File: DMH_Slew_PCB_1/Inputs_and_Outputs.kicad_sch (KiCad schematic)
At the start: 35 parts, among them J1 TS_Jack_6.35mm_Sw, J10 TS_Jack_6.35mm_Sw, J11 TS_Jack_6.35mm_Sw, J2 TS_Jack_6.35mm_Sw, J200 IDC_02x05, J3 TS_Jack_6.35mm_Sw, J4 TS_Jack_6.35mm_Sw, J5 TS_Jack_6.35mm_Sw, J6 TS_Jack_6.35mm_Sw, J7 TS_Jack_6.35mm_Sw, J8 TS_Jack_6.35mm_Sw, J9 TS_Jack_6.35mm_Sw, SW3 SW_SPDT, U1 TL074, U2 TL072, U5 CD4053B, U6 CD4053B

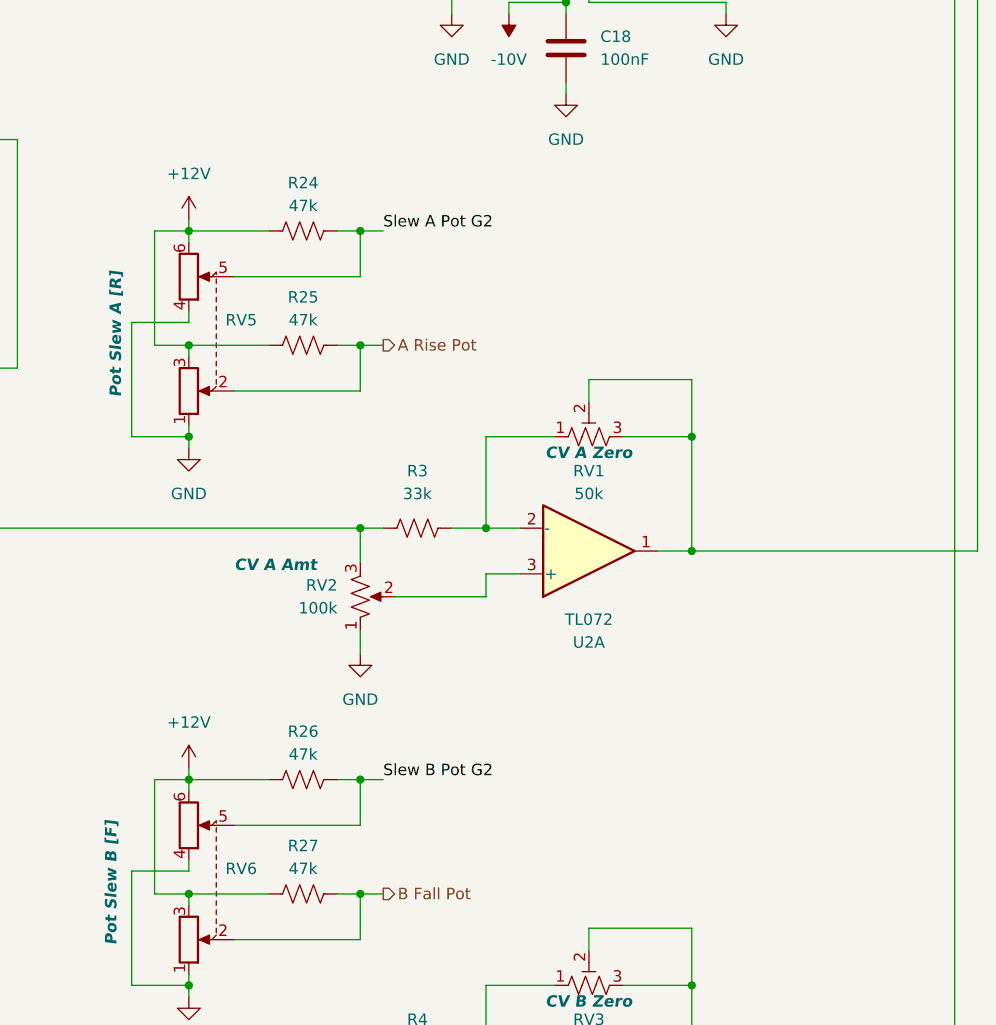
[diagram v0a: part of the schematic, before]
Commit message: Applied 10V to pots
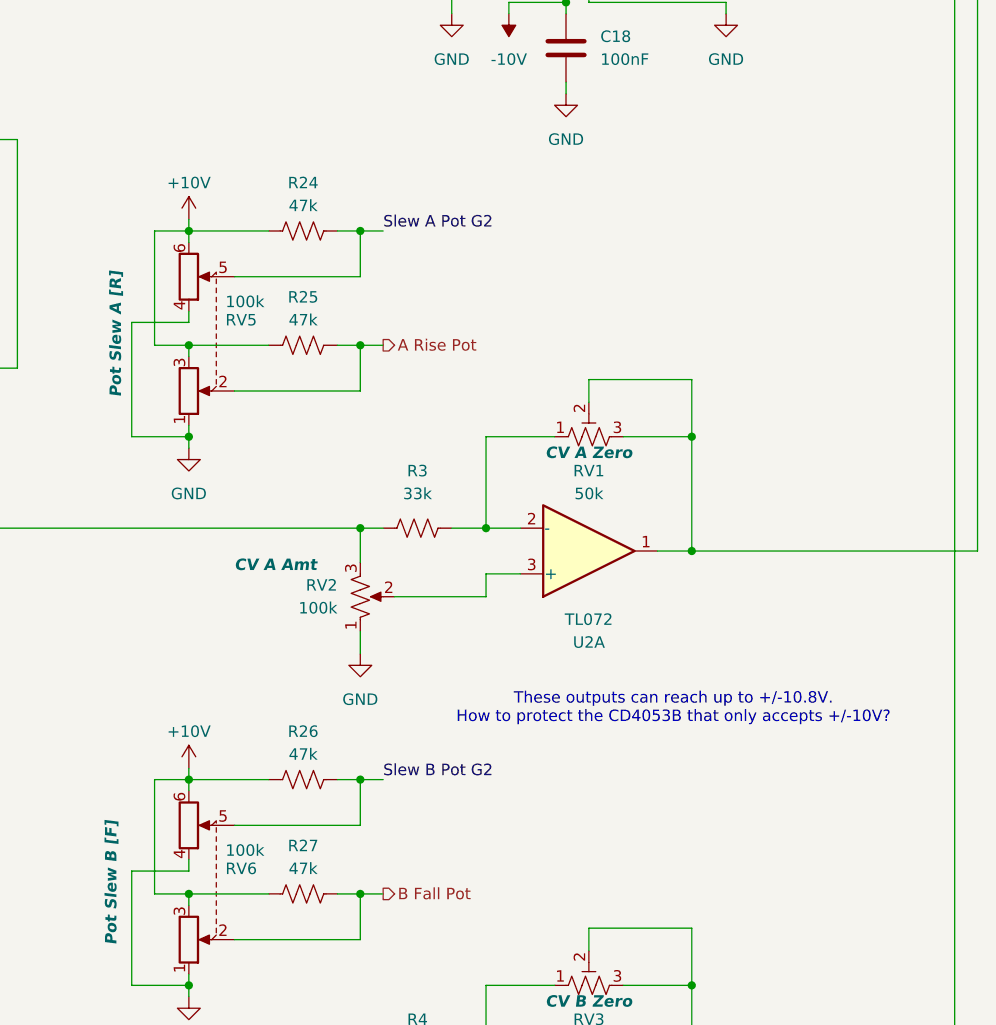
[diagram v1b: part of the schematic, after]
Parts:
- RV5, RV6: value R_Potentiometer_Dual -> 100k
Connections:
- net +12V is gone; now on net +10V: R24.1, R25.1, R26.1, R27.1, RV5.3, RV5.6, RV6.3, RV6.6
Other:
- note added: "These outputs can reach up to +/-10.8V. How to protect the CD4053B that only accepts +/-10V?"
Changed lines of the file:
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@@
 		(comment 1 "PCB for 5 cm Kosmo format synthesizer module")
 	)
+	(text "These outputs can reach up to +/-10.8V.\nHow to protect the CD4053B that only accepts +/-10V?"
+		(exclude_from_sim no)
+		(at 161.798 192.786 0)
+		(effects
+			(font
+				(size 1.27 1.27)
+			)
+		)
+	)
 	(junction
 		(at 127 139.7)
@@
 	)
 	(symbol
+		(lib_id "power:+10V")
+		(at 107.95 138.43 0)
+		(unit 1)
+		(exclude_from_sim no)
+		(in_bom yes)
+		(on_board yes)
+		(dnp no)
+		(property "Reference" "#PWR024"
+			(at 107.95 142.24 0)
+			(effects
+				(font
+					(size 1.27 1.27)
+				)
+				(hide yes)
+			)
+		)
+		(property "Value" "+10V"
+			(at 107.95 134.366 0)
+			(effects
+				(font
+					(size 1.27 1.27)
+				)
+			)
+		)
+		(property "Footprint" ""
+			(at 107.95 138.43 0)
+			(effects
+				(font
+					(size 1.27 1.27)
+				)
+				(hide yes)
+			)
+		)
+		(property "Datasheet" ""
+			(at 107.95 138.43 0)
+			(effects
+				(font
+					(size 1.27 1.27)
+				)
+				(hide yes)
+			)
+		)
+		(property "Description" "Power symbol creates a global label with name \"+10V\""
+			(at 107.95 138.43 0)
+			(effects
+				(font
+					(size 1.27 1.27)
+				)
+				(hide yes)
+			)
+		)
+		(pin "1"
+		)
+		(instances
+			(project "DMH_Slew_PCB_1"
+				(path "/58f4306d-5387-4983-bb08-41a2313fd315/ce3fef8b-9f1d-4178-b50b-4a046c030679"
+					(reference "#PWR024")
+					(unit 1)
+				)
+			)
+		)
+	)
+	(symbol
 		(lib_id "Device:R_US")
 		(at 120.65 152.4 90)
@@
 	)
 	(symbol
-		(lib_id "SynthStuff:TS_Jack_6.35mm_Sw")
-		(at 25.4 152.4 0)
+		(lib_id "power:+10V")
+		(at 107.95 199.39 0)
 		(unit 1)
 		(exclude_from_sim no)
@@
 		(on_board yes)
 		(dnp no)
-		(property "Reference" "J6"
-			(at 24.765 143.51 0)
+		(property "Reference" "#PWR026"
+			(at 107.95 203.2 0)
 			(effects
 				(font
 					(size 1.27 1.27)
 				)
+				(hide yes)
 			)
 		)
-		(property "Value" "TS_Jack_6.35mm_Sw"
-			(at 24.765 146.05 0)
+		(property "Value" "+10V"
+			(at 107.95 195.326 0)
 			(effects
 				(font
@@
 			)
 		)
-		(property "Footprint" "SynthStuff:CUI_MJ-63052A"
-			(at 25.4 152.4 0)
+		(property "Footprint" ""
+			(at 107.95 199.39 0)
 			(effects
 				(font
@@
 			)
 		)
-		(property "Datasheet" "~"
-			(at 25.4 152.4 0)
+		(property "Datasheet" ""
+			(at 107.95 199.39 0)
 			(effects
 				(font
@@
 			)
 		)
-		(property "Description" "Audio Jack, 2 Poles (Mono / TS), Switched T Pole (Normalling), 6.35mm, 1/4inch"
-			(at 25.4 152.4 0)
+		(property "Description" "Power symbol creates a global label with name \"+10V\""
+			(at 107.95 199.39 0)
 			(effects
 				(font
@@
 			)
 		)
-		(property "Function" "Slew A In"
-			(at 25.4 159.512 0)
-			(effects
-				(font
-					(size 1.27 1.27)
-					(thickness 0.254)
-					(bold yes)
-					(italic yes)
-				)
-			)
-		)
-		(pin "TN"
-		)
-		(pin "S"
-		)
-		(pin "T"
+		(pin "1"
 		)
 		(instances
 			(project "DMH_Slew_PCB_1"
 				(path "/58f4306d-5387-4983-bb08-41a2313fd315/ce3fef8b-9f1d-4178-b50b-4a046c030679"
-					(reference "J6")
+					(reference "#PWR026")
 					(unit 1)
 				)
@@
 	)
 	(symbol
-		(lib_id "power:+12V")
-		(at 107.95 138.43 0)
+		(lib_id "SynthStuff:TS_Jack_6.35mm_Sw")
+		(at 25.4 152.4 0)
 		(unit 1)
 		(exclude_from_sim no)
@@
 		(on_board yes)
 		(dnp no)
-		(fields_autoplaced yes)
-		(property "Reference" "#PWR024"
-			(at 107.95 142.24 0)
+		(property "Reference" "J6"
+			(at 24.765 143.51 0)
 			(effects
 				(font
 					(size 1.27 1.27)
 				)
-				(hide yes)
 			)
 		)
-		(property "Value" "+12V"
-			(at 107.95 133.35 0)
+		(property "Value" "TS_Jack_6.35mm_Sw"
+			(at 24.765 146.05 0)
 			(effects
 				(font
@@
 			)
 		)
-		(property "Footprint" ""
-			(at 107.95 138.43 0)
+		(property "Footprint" "SynthStuff:CUI_MJ-63052A"
+			(at 25.4 152.4 0)
 			(effects
 				(font
@@
 			)
 		)
-		(property "Datasheet" ""
-			(at 107.95 138.43 0)
+		(property "Datasheet" "~"
+			(at 25.4 152.4 0)
 			(effects
 				(font
@@
 			)
 		)
-		(property "Description" "Power symbol creates a global label with name \"+12V\""
-			(at 107.95 138.43 0)
+		(property "Description" "Audio Jack, 2 Poles (Mono / TS), Switched T Pole (Normalling), 6.35mm, 1/4inch"
+			(at 25.4 152.4 0)
 			(effects
 				(font
@@
 			)
 		)
-		(pin "1"
+		(property "Function" "Slew A In"
+			(at 25.4 159.512 0)
+			(effects
+				(font
+					(size 1.27 1.27)
+					(thickness 0.254)
+					(bold yes)
+					(italic yes)
+				)
+			)
+		)
+		(pin "TN"
+		)
+		(pin "S"
+		)
+		(pin "T"
 		)
 		(instances
 			(project "DMH_Slew_PCB_1"
 				(path "/58f4306d-5387-4983-bb08-41a2313fd315/ce3fef8b-9f1d-4178-b50b-4a046c030679"
-					(reference "#PWR024")
+					(reference "J6")
 					(unit 1)
 				)
@@
 			)
 		)
-		(property "Value" "R_Potentiometer_Dual"
-			(at 112.776 208.534 90)
+		(property "Value" "100k"
+			(at 112.014 208.534 90)
 			(effects
 				(font
@@
 				)
 				(justify left)
-				(hide yes)
 			)
 		)
@@
 			)
 		)
-		(property "Value" "R_Potentiometer_Dual"
-			(at 112.776 147.574 90)
+		(property "Value" "100k"
+			(at 112.014 147.574 90)
 			(effects
 				(font
@@
 				)
 				(justify left)
-				(hide yes)
 			)
 		)
@@
 					(unit 1)
 				)
-			)
-		)
-	)
-	(symbol
-		(lib_id "power:+12V")
-		(at 107.95 199.39 0)
-		(unit 1)
-		(exclude_from_sim no)
-		(in_bom yes)
-		(on_board yes)
-		(dnp no)
-		(fields_autoplaced yes)
-		(property "Reference" "#PWR026"
-			(at 107.95 203.2 0)
-			(effects
-				(font
-					(size 1.27 1.27)
-				)
-				(hide yes)
-			)
-		)
-		(property "Value" "+12V"
-			(at 107.95 194.31 0)
-			(effects
-				(font
-					(size 1.27 1.27)
-				)
-			)
-		)
-		(property "Footprint" ""
-			(at 107.95 199.39 0)
-			(effects
-				(font
-					(size 1.27 1.27)
-				)
-				(hide yes)
-			)
-		)
-		(property "Datasheet" ""
-			(at 107.95 199.39 0)
-			(effects
-				(font
-					(size 1.27 1.27)
-				)
-				(hide yes)
-			)
-		)
-		(property "Description" "Power symbol creates a global label with name \"+12V\""
-			(at 107.95 199.39 0)
-			(effects
-				(font
-					(size 1.27 1.27)
-				)
-				(hide yes)
-			)
-		)
-		(pin "1"
-		)
-		(instances
-			(project "DMH_Slew_PCB_1"
-				(path "/58f4306d-5387-4983-bb08-41a2313fd315/ce3fef8b-9f1d-4178-b50b-4a046c030679"
-					(reference "#PWR026")
-					(unit 1)
-				)

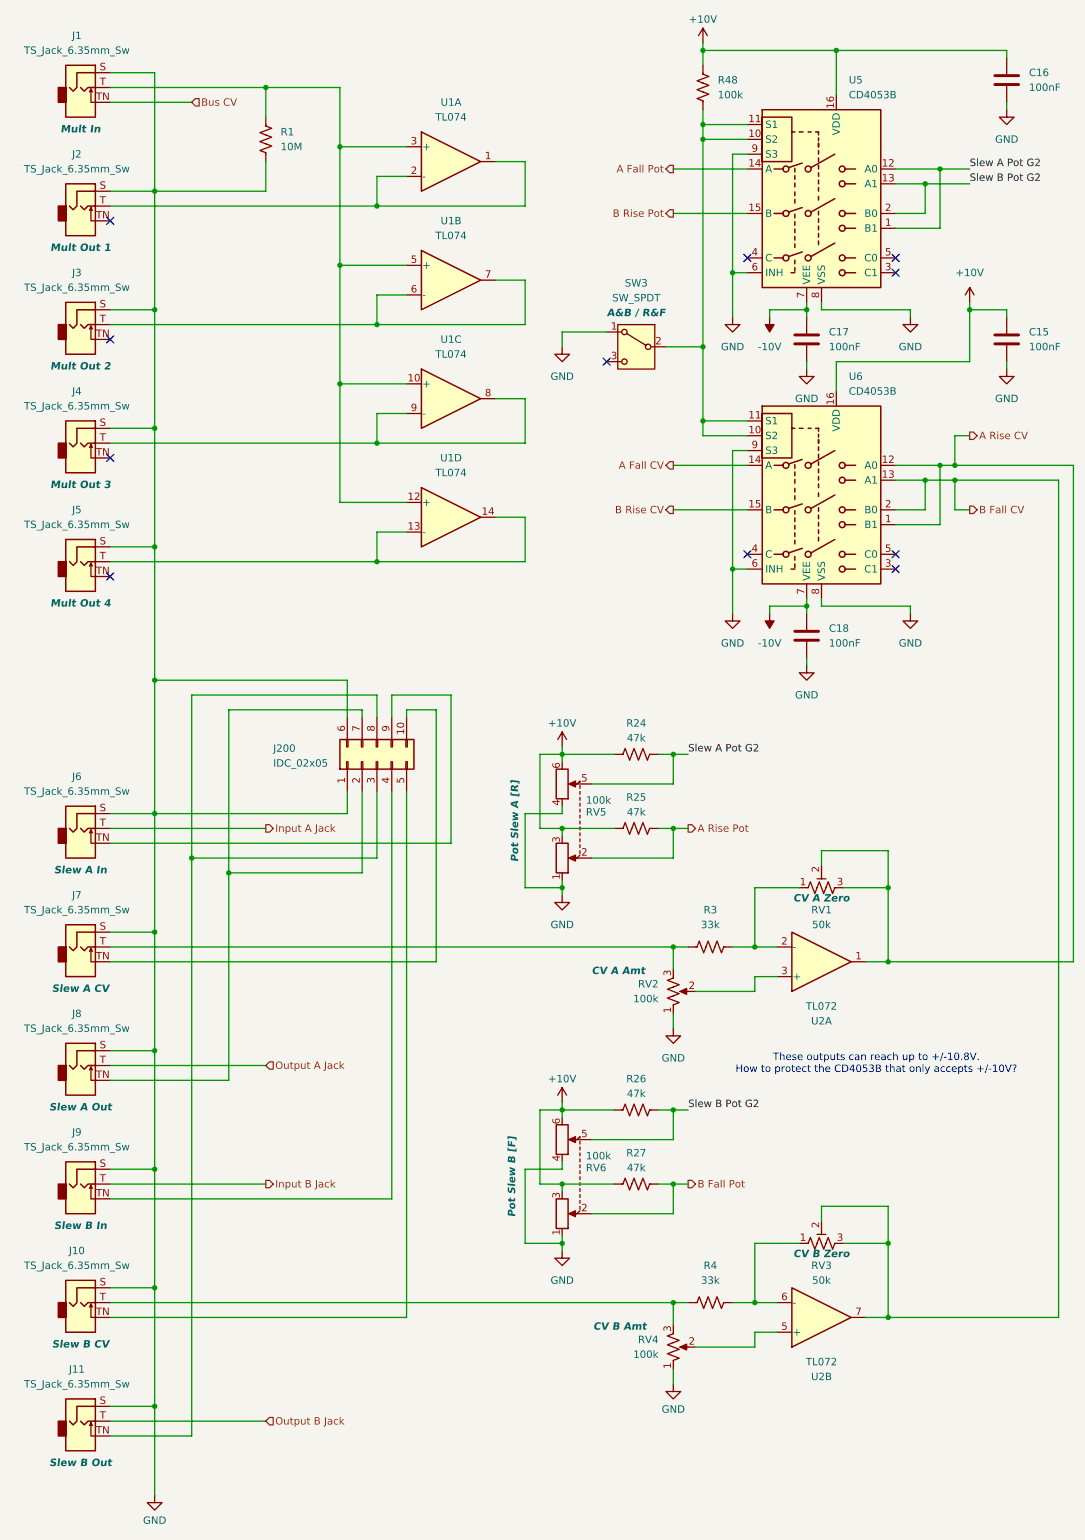
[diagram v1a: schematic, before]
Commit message: Added zeners to limit CV inputs to CD4053B
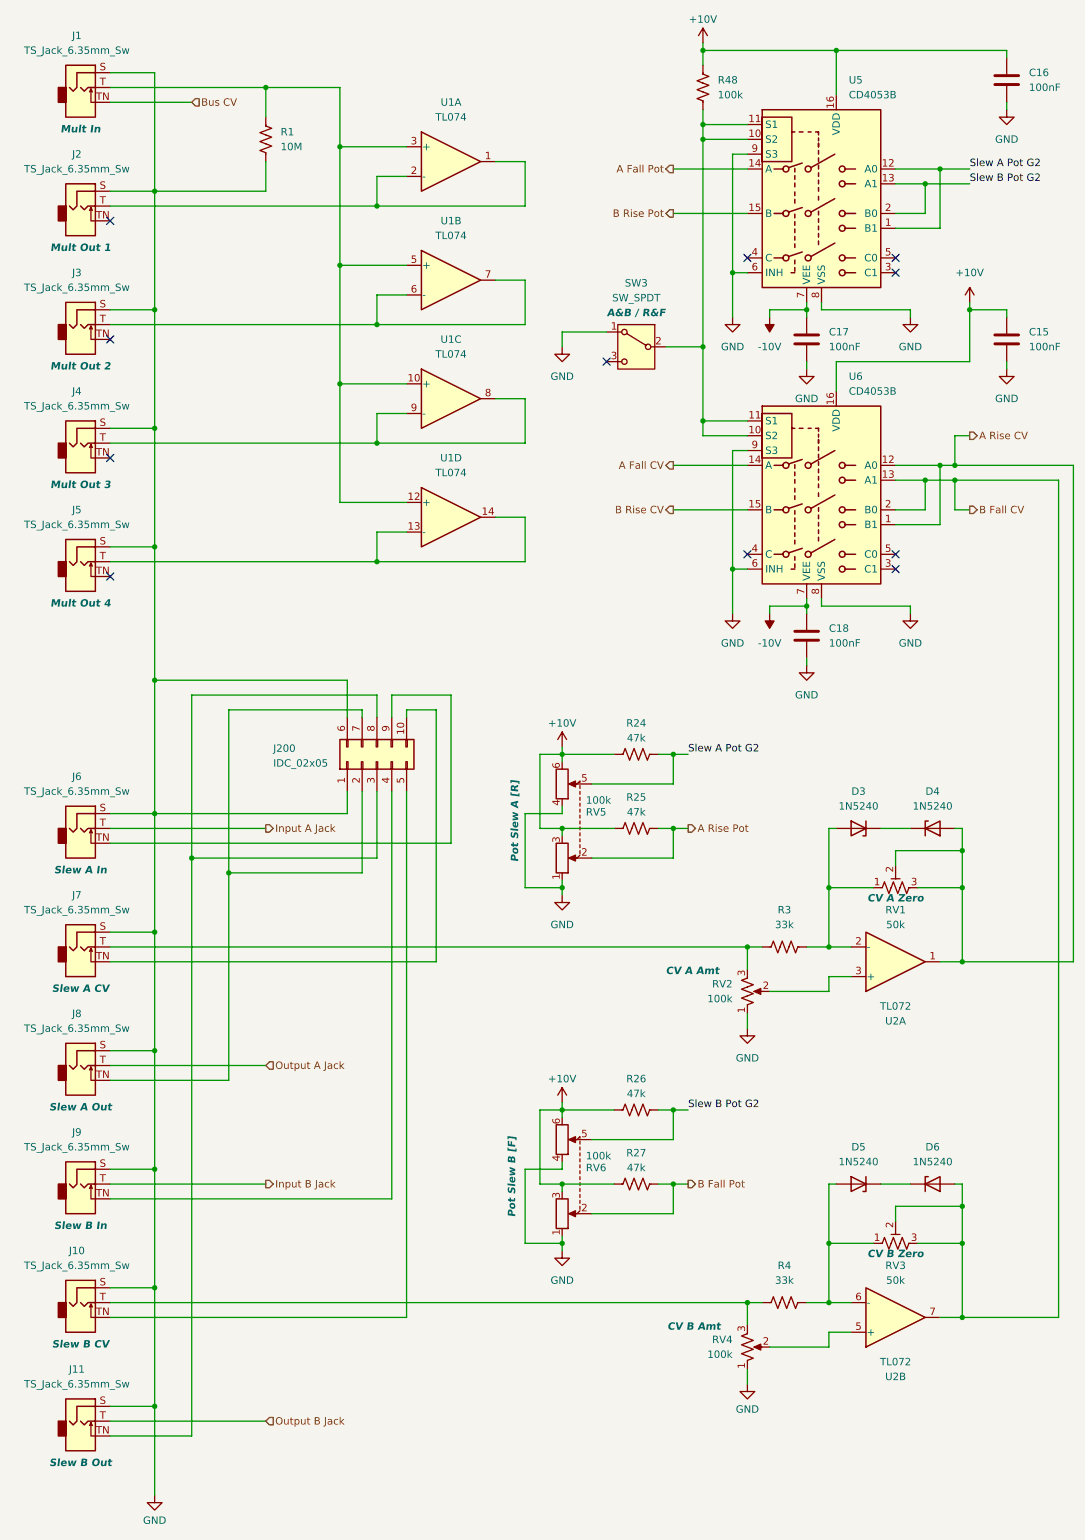
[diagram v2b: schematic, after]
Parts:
- added D3, D4, D5, D6: 1N5240, Diode_THT:D_DO-35_SOD27_P7.62mm_Horizontal, symbol Device:D_Zener
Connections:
- net A Rise CV: now also D4.2 (A)
- net B Fall CV: now also D6.2 (A)
- net at R4.2, RV3.1, U2.6 (-): now also D5.2 (A)
- net at R3.2, RV1.1, U2.2 (-): now also D3.2 (A)
- new net: D3.1 (K), D4.1 (K)
- new net: D5.1 (K), D6.1 (K)
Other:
- note removed: "These outputs can reach up to +/-10.8V. How to protect the CD4053B that only accepts +/-10V?"
- moved on the sheet: R3, R4, RV1, RV2, RV3, RV4, U2A, U2B

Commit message: Exported preliminary BoM
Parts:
- SW3: footprint (none) -> SynthStuff:Toggle_Switch_TE
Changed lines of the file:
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@@
 			)
 		)
-		(property "Footprint" ""
+		(property "Footprint" "SynthStuff:Toggle_Switch_TE"
 			(at 120.65 69.85 0)
 			(effects

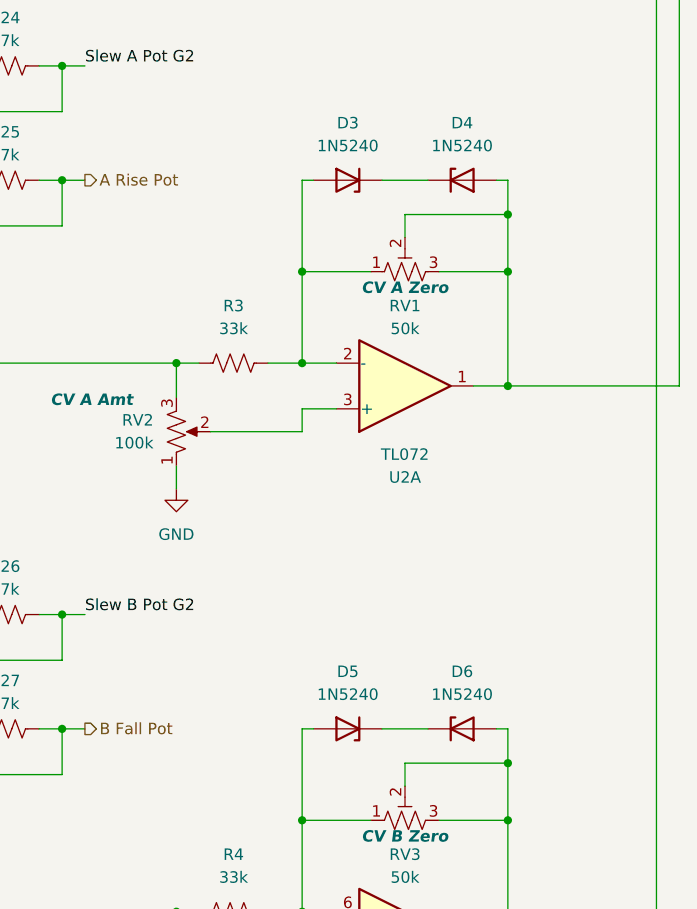
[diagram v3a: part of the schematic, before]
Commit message: Update Inputs_and_Outputs.kicad_sch
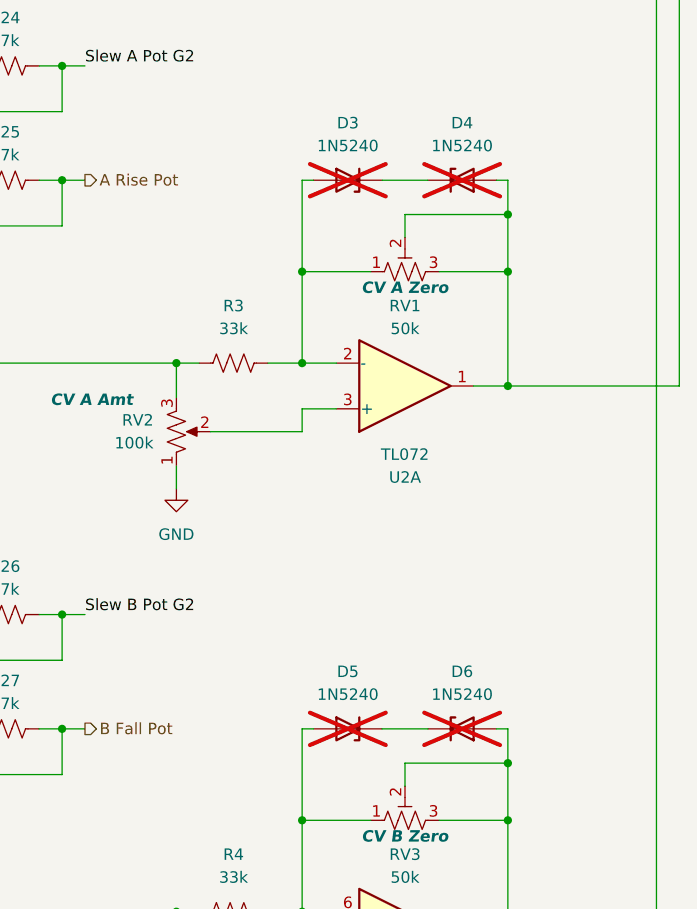
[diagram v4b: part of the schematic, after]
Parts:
- D3, D4, D5, D6: now not fitted
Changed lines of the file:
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@@
 		(in_bom yes)
 		(on_board yes)
-		(dnp no)
+		(dnp yes)
 		(fields_autoplaced yes)
 		(property "Reference" "D3"
@@
 		(in_bom yes)
 		(on_board yes)
-		(dnp no)
+		(dnp yes)
 		(fields_autoplaced yes)
 		(property "Reference" "D5"
@@
 		(in_bom yes)
 		(on_board yes)
-		(dnp no)
+		(dnp yes)
 		(fields_autoplaced yes)
 		(property "Reference" "D4"
@@
 		(in_bom yes)
 		(on_board yes)
-		(dnp no)
+		(dnp yes)
 		(fields_autoplaced yes)
 		(property "Reference" "D6"
